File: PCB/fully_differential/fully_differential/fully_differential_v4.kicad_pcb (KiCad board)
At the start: 2 copper layers, 127.5 x 90.7 mm, 35 parts, among them J1 Conn_01x02, J2 Conn_01x03, J3 Conn_01x03, U1 LM324, U2 LM324, U3 LM358, U4 AD8138ARZ, U5 L7805, U6 L7905

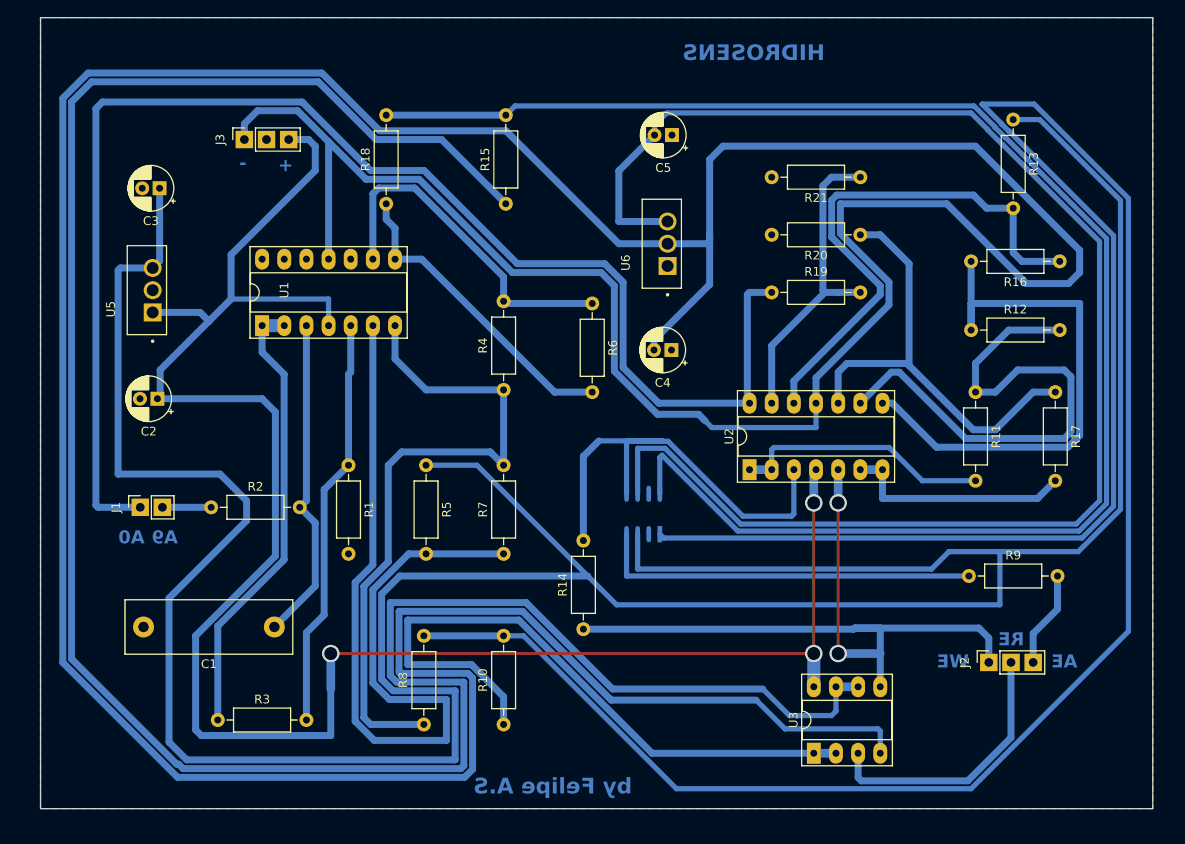
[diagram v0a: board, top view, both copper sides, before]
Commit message: fix proteus 1.5v and 3v
stock v2 proteus and kicad ok
fully v4 proteus and kicad ok
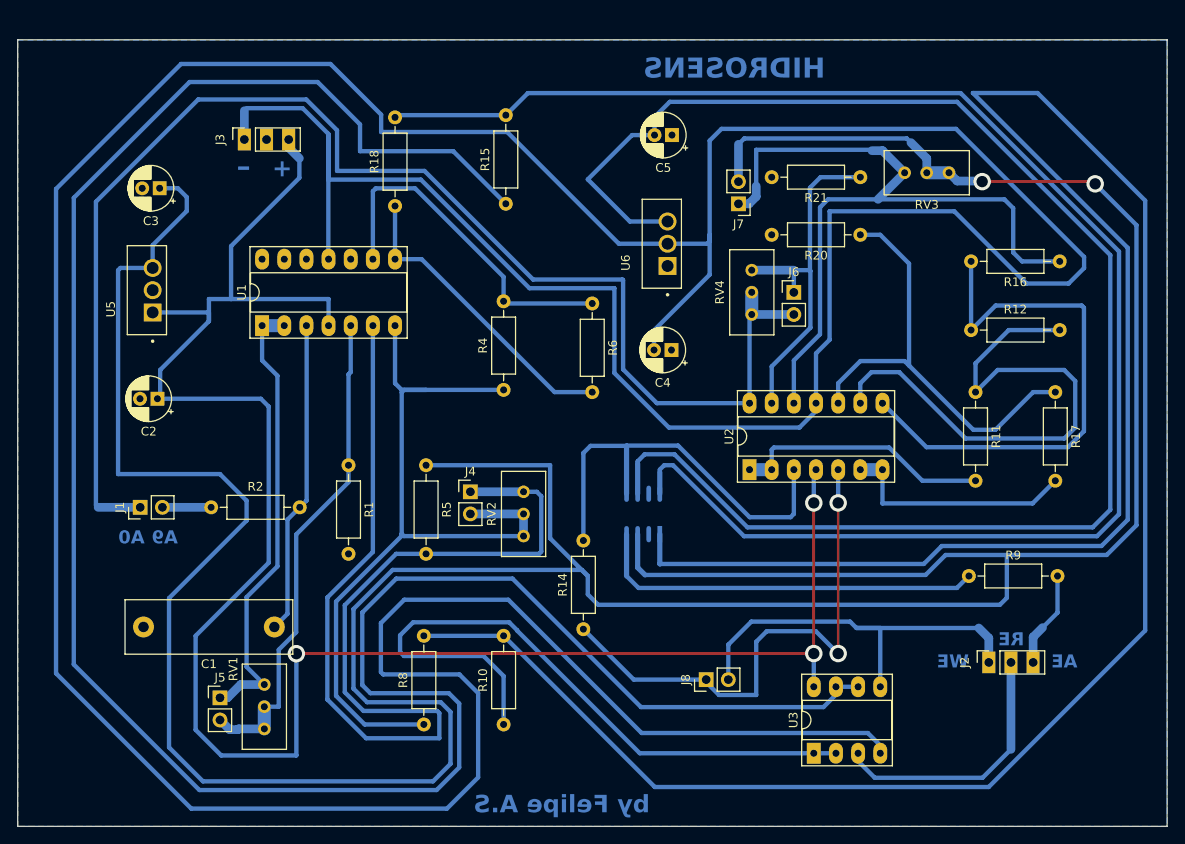
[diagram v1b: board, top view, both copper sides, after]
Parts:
- removed R13: 3.3K, Resistor_THT:R_Axial_DIN0207_L6.3mm_D2.5mm_P10.16mm_Horizontal
- removed R19: 1.17K, Resistor_THT:R_Axial_DIN0207_L6.3mm_D2.5mm_P10.16mm_Horizontal
- removed R3: 2.83K, Resistor_THT:R_Axial_DIN0207_L6.3mm_D2.5mm_P10.16mm_Horizontal
- removed R7: 150, Resistor_THT:R_Axial_DIN0207_L6.3mm_D2.5mm_P10.16mm_Horizontal
- added J4: Conn_01x02, Connector_PinHeader_2.54mm:PinHeader_1x02_P2.54mm_Vertical, F.Cu at (125.0, 102.1)
- added J5: Conn_01x02, Connector_PinHeader_2.54mm:PinHeader_1x02_P2.54mm_Vertical, F.Cu at (96.3, 125.7)
- added J6: Conn_01x02, Connector_PinHeader_2.54mm:PinHeader_1x02_P2.54mm_Vertical, F.Cu at (162.1, 79.2)
- added J7: Conn_01x02, Connector_PinHeader_2.54mm:PinHeader_1x02_P2.54mm_Vertical, F.Cu at (155.7, 69.1)
- added J8: Conn_01x02, Connector_PinHeader_2.54mm:PinHeader_1x02_P2.54mm_Vertical, F.Cu at (152.0, 123.6)
- added RV1: R_Potentiometer_Trim, Potentiometer_THT:Potentiometer_Bourns_3296W_Vertical, F.Cu at (101.3, 124.2)
- added RV2: R_Potentiometer_Trim, Potentiometer_THT:Potentiometer_Bourns_3296W_Vertical, F.Cu at (131.1, 102.1)
- added RV3: R_Potentiometer_Trim, Potentiometer_THT:Potentiometer_Bourns_3296W_Vertical, F.Cu at (174.8, 65.5)
- added RV4: R_Potentiometer_Trim, Potentiometer_THT:Potentiometer_Bourns_3296W_Vertical, F.Cu at (157.2, 76.7)
- J1: footprint Connector_PinSocket_2.54mm:PinSocket_1x02_P2.54mm_Vertical -> Connector_PinHeader_2.54mm:PinHeader_1x02_P2.54mm_Vertical
- moved R18 1.05 mm to (116.3, 69.3)
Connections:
- R14 pad 1: Net-(J2-Pin_1) -> Net-(J8-Pin_1)
- U2 pad 5: Net-(J2-Pin_1) -> Net-(J8-Pin_1)
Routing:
- net Net-(J8-Pin_1): track 0.00 -> 61.2 mm, vias 0 -> 2
- net +5V: track 361.3 -> 417.7 mm, vias 0 -> 2
- net Net-(J2-Pin_1): track 85.4 -> 48.0 mm, vias 2 -> 0
- net Net-(J7-Pin_1): track 62.2 -> 87.6 mm
- net Net-(J4-Pin_1): track 98.9 -> 124.1 mm
- net t+: track 78.1 -> 94.3 mm
- net Net-(U4--IN): track 272.5 -> 286.9 mm
- net Net-(J5-Pin_2): track 47.3 -> 56.9 mm
- net -9V: track 531.8 -> 539.3 mm
- net -5V: track 168.7 -> 174.9 mm
- net Net-(J6-Pin_1): track 36.3 -> 42.0 mm
- net Net-(U2A-+): track 53.5 -> 48.6 mm
- net Net-(U2C--): track 62.2 -> 64.0 mm
- net +9V: track 220.7 -> 222.4 mm
- net Net-(U4-+IN): track 180.1 -> 181.8 mm
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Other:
- board size 127.5 x 90.7 mm -> 131.8 x 90.2 mm
